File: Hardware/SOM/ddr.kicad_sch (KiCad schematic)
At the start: 25 parts, among them U2 AS4C256M16D3

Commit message: DDR Banks Vref
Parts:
- added C57: 1uF, Capacitor_SMD:C_0402_1005Metric, symbol RA8M1:885012205092
- added C58: 100nF, Capacitor_SMD:C_0402_1005Metric, symbol RA8M1:885012205092
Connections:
- net DDR_VREF: now also C57.2, C58.2
- net GND: now also C57.1, C58.1
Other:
- moved on the sheet: R11, R12, R13, R4, R5

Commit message: SOM: power supplies
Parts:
- removed L1, L2: 600R, Inductor_SMD:L_0402_1005Metric, symbol Device:L
- added FB2, FB3: FerriteBead, Inductor_SMD:L_0402_1005Metric, symbol Device:FerriteBead
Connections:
- net 1.5V: now also FB2.1, FB3.1
- net DDR_VDDQ_1.5V: now also FB2.2
- net DDR_VDD_1.5V: now also FB3.2

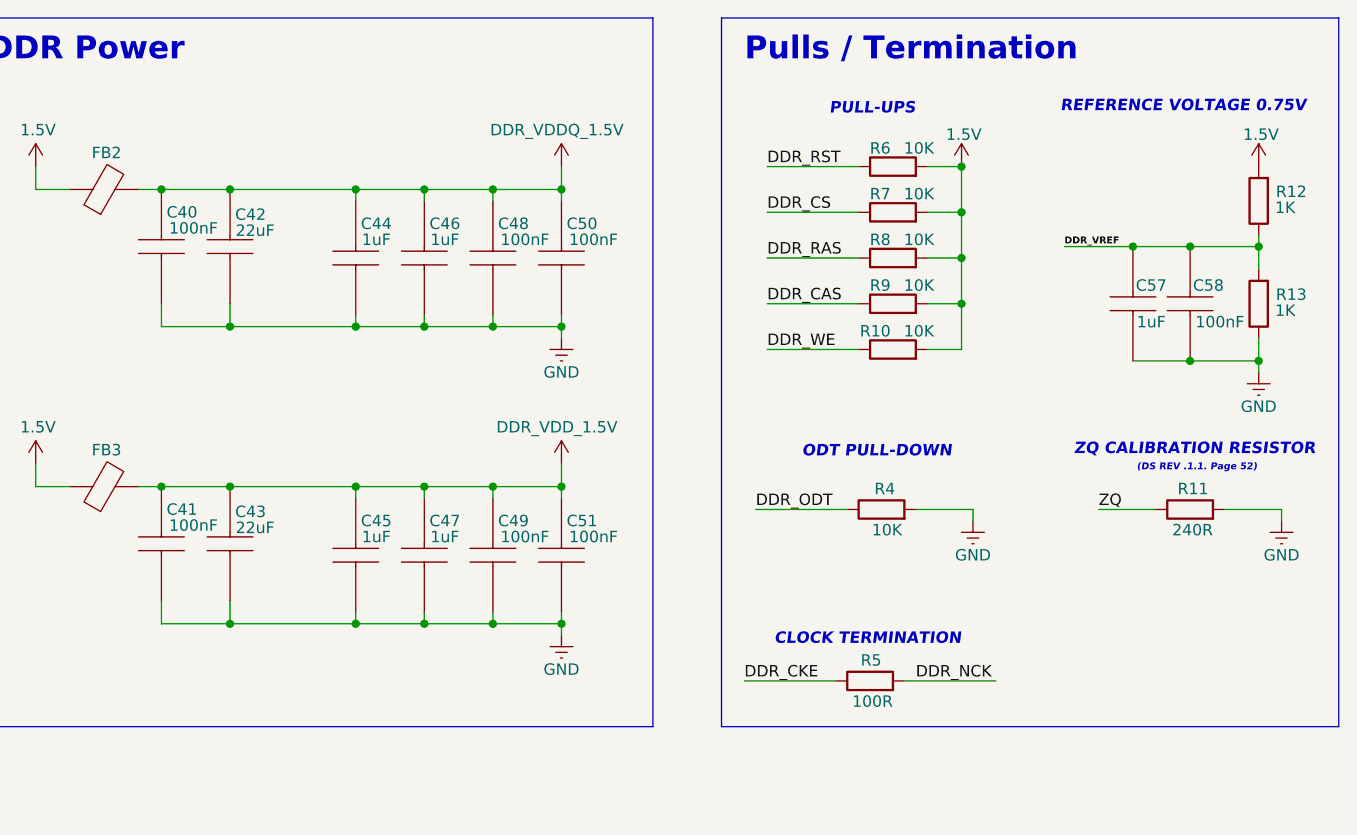
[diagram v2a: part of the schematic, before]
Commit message: SOM: power supply update
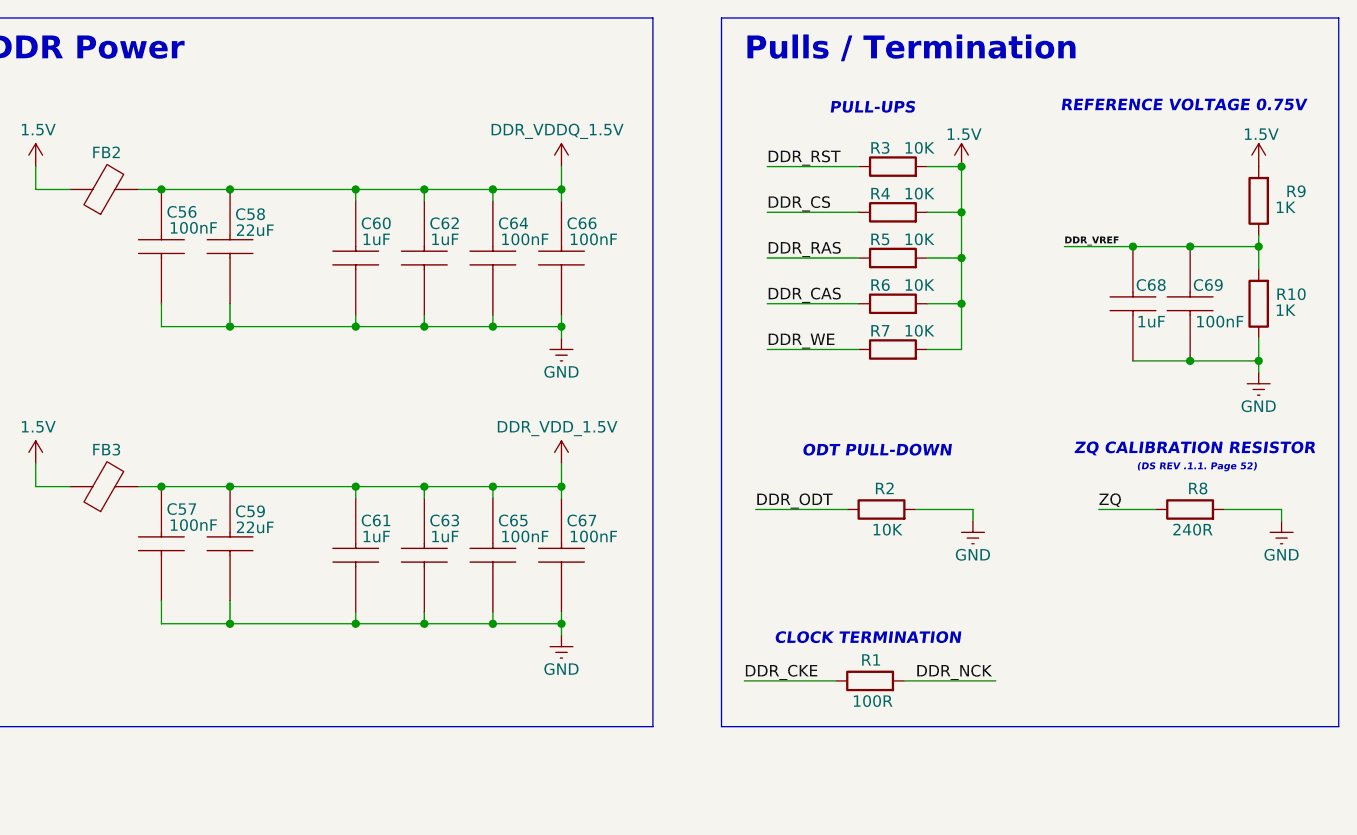
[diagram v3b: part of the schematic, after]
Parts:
- renumbered C40 to C56, C41 to C57, C42 to C58, C43 to C59, C44 to C60, C45 to C61, C46 to C62, C47 to C63, C48 to C64, C49 to C65, C50 to C66, C51 to C67, C57 to C68, C58 to C69, R5 to R1, R13 to R10, R4 to R2, R6 to R3, R7 to R4, R8 to R5, R9 to R6, R10 to R7, R11 to R8, R12 to R9

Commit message: SOM: layout update
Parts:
- renumbered C56 to C76, C57 to C77, C58 to C78, C59 to C79, C60 to C80, C61 to C81, C62 to C82, C63 to C83, C64 to C84, C65 to C85, C66 to C86, C67 to C87, C68 to C88, C69 to C89, FB2 to FB8, FB3 to FB9
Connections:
- net DDR_CKE: no longer U2.K9 (CKE)
- net DDR_NCK: no longer U2.K7 (~{CK})
- new net DDR_CK_N: U2.K7 (~{CK})
- new net DDR_CK_P: U2.K9 (CKE)

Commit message: SOM: layout update
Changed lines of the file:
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@@
 		(dnp no)
 		(property "Reference" "R9"
-			(at 272.034 40.894 0)
+			(at 270.764 40.894 0)
 			(effects
 				(font

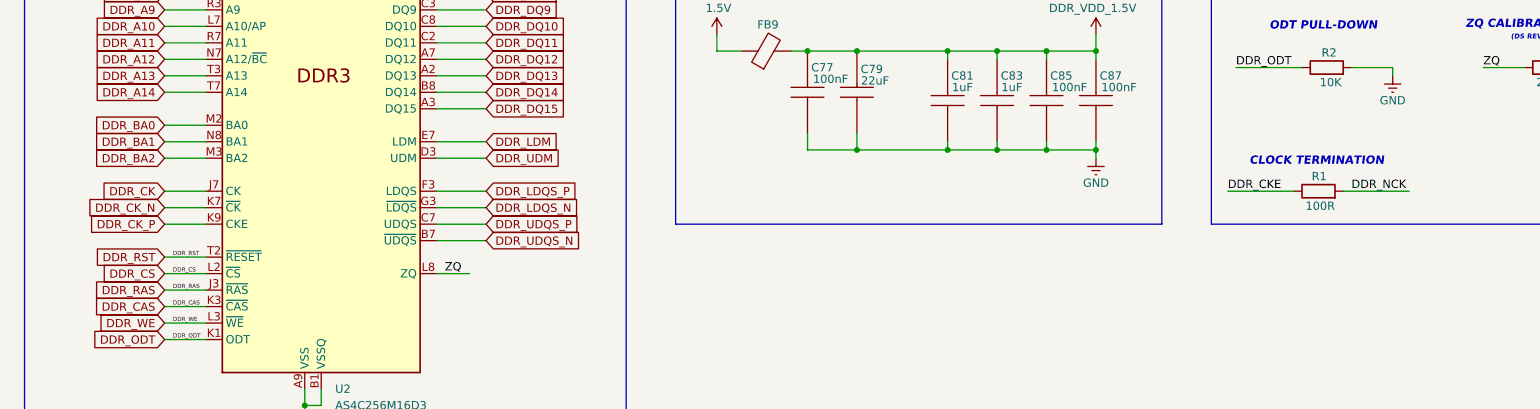
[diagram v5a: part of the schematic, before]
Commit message: DDR clock schematics fixed
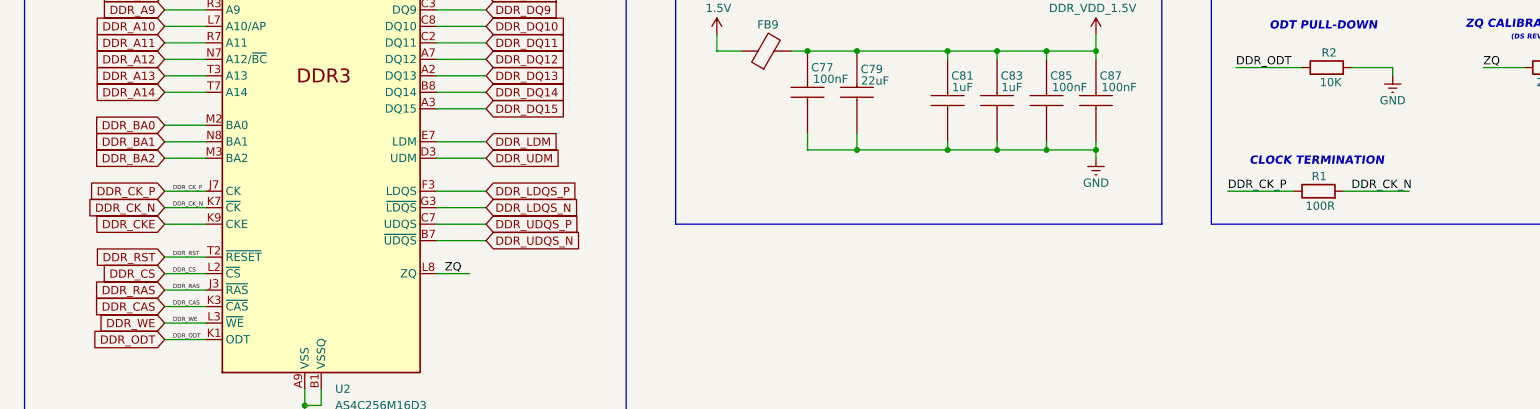
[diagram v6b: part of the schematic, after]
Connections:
- net DDR_CK is gone; now on net DDR_CK_P: U2.J7 (CK)
- net DDR_NCK is gone; now on net DDR_CK_N: R1.2
- net DDR_CKE: now also U2.K9 (CKE); no longer R1.1
- net DDR_CK_P: now also R1.1; no longer U2.K9 (CKE)
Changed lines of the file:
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@@
+		)
+	)
+	(label "DDR_CK_P"
+		(at 46.99 95.25 0)
+		(effects
+			(font
+				(size 0.635 0.635)
+			)
+			(justify left bottom)
 		)
 	)
@@
 		)
 	)
-	(label "DDR_NCK"
+	(label "DDR_CK_N"
+		(at 46.99 97.79 0)
+		(effects
+			(font
+				(size 0.635 0.635)
+			)
+			(justify left bottom)
+		)
+	)
+	(label "DDR_CK_N"
 		(at 228.6 95.25 0)
 		(effects
@@
 		)
 	)
-	(label "DDR_CKE"
+	(label "DDR_CK_P"
 		(at 209.55 95.25 0)
 		(effects
@@
 		)
 	)
+	(global_label "DDR_CKE"
+		(shape input)
+		(at 45.72 100.33 180)
+		(fields_autoplaced yes)
+		(effects
+			(font
+				(size 1.27 1.27)
+			)
+			(justify right)
+		)
+		(property "Intersheetrefs" "${INTERSHEET_REFS}"
+			(at 34.2682 100.33 0)
+			(effects
+				(font
+					(size 1.27 1.27)
+				)
+				(justify right)
+				(hide yes)
+			)
+		)
+	)
+	(global_label "DDR_DQ9"
+		(shape input)
+		(at 95.25 67.31 0)
+		(fields_autoplaced yes)
+		(effects
+			(font
+				(size 1.27 1.27)
+			)
+			(justify left)
+		)
+		(property "Intersheetrefs" "${INTERSHEET_REFS}"
+			(at 106.8228 67.31 0)
+			(effects
+				(font
+					(size 1.27 1.27)
+				)
+				(justify left)
+				(hide yes)
+			)
+		)
+	)
+	(global_label "DDR_DQ13"
+		(shape input)
+		(at 95.25 77.47 0)
+		(fields_autoplaced yes)
+		(effects
+			(font
+				(size 1.27 1.27)
+			)
+			(justify left)
+		)
+		(property "Intersheetrefs" "${INTERSHEET_REFS}"
+			(at 108.0323 77.47 0)
+			(effects
+				(font
+					(size 1.27 1.27)
+				)
+				(justify left)
+				(hide yes)
+			)
+		)
+	)
 	(global_label "DDR_CK_P"
 		(shape input)
-		(at 45.72 100.33 180)
-		(fields_autoplaced yes)
-		(effects
-			(font
-				(size 1.27 1.27)
-			)
-			(justify right)
-		)
-		(property "Intersheetrefs" "${INTERSHEET_REFS}"
-			(at 33.1796 100.33 0)
-			(effects
-				(font
-					(size 1.27 1.27)
-				)
-				(justify right)
-				(hide yes)
-			)
-		)
-	)
-	(global_label "DDR_DQ9"
-		(shape input)
-		(at 95.25 67.31 0)
-		(fields_autoplaced yes)
-		(effects
-			(font
-				(size 1.27 1.27)
-			)
-			(justify left)
-		)
-		(property "Intersheetrefs" "${INTERSHEET_REFS}"
-			(at 106.8228 67.31 0)
-			(effects
-				(font
-					(size 1.27 1.27)
-				)
-				(justify left)
-				(hide yes)
-			)
-		)
-	)
-	(global_label "DDR_DQ13"
-		(shape input)
-		(at 95.25 77.47 0)
-		(fields_autoplaced yes)
-		(effects
-			(font
-				(size 1.27 1.27)
-			)
-			(justify left)
-		)
-		(property "Intersheetrefs" "${INTERSHEET_REFS}"
-			(at 108.0323 77.47 0)
-			(effects
-				(font
-					(size 1.27 1.27)
-				)
-				(justify left)
-				(hide yes)
-			)
-		)
-	)
-	(global_label "DDR_CK"
-		(shape input)
 		(at 45.72 95.25 180)
 		(fields_autoplaced yes)
@@
 		)
 		(property "Intersheetrefs" "${INTERSHEET_REFS}"
-			(at 35.4172 95.25 0)
-			(effects
-				(font
+			(at 33.1796 95.25 0)
+			(effects
+				(font

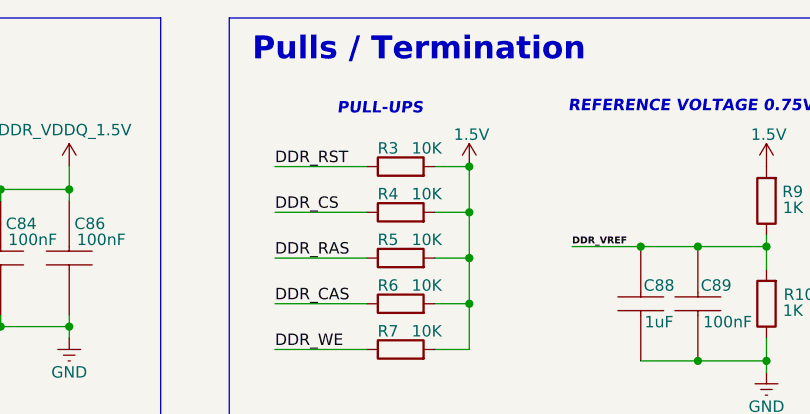
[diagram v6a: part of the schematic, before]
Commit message: SOM: DDR PWR UPD
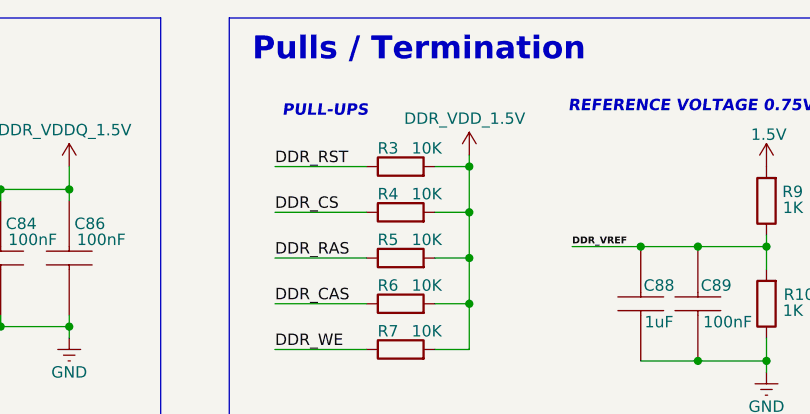
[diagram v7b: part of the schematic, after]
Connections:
- net 1.5V: no longer R3.2, R4.2, R5.2, R6.2, R7.2
- net DDR_VDD_1.5V: now also R3.2, R4.2, R5.2, R6.2, R7.2
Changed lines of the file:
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@@
 	(text "PULL-UPS"
 		(exclude_from_sim no)
-		(at 223.774 31.75 0)
+		(at 217.678 32.004 0)
 		(effects
 			(font
@@
 	)
 	(junction
+		(at 233.68 38.1)
+		(diameter 0)
+		(color 0 0 0 0)
+	)
+	(junction
 		(at 189.23 55.88)
 		(diameter 0)
@@
 	)
 	(junction
-		(at 233.68 38.1)
-		(diameter 0)
-		(color 0 0 0 0)
-	)
-	(junction
 		(at 74.93 35.56)
 		(diameter 0)
@@
 	(wire
 		(pts
+			(xy 233.68 36.83) (xy 233.68 38.1)
+		)
+		(stroke
+			(width 0)
+			(type default)
+		)
+	)
+	(wire
+		(pts
 			(xy 45.72 62.23) (xy 52.07 62.23)
 		)
@@
 	)
 	(symbol
-		(lib_id "power:+1V5")
-		(at 233.68 38.1 0)
-		(unit 1)
-		(exclude_from_sim no)
-		(in_bom yes)
-		(on_board yes)
-		(dnp no)
-		(property "Reference" "#PWR062"
-			(at 233.68 41.91 0)
-			(effects
-				(font
-					(size 1.27 1.27)
-				)
-				(hide yes)
-			)
-		)
-		(property "Value" "1.5V"
-			(at 233.934 34.544 0)
-			(effects
-				(font
-					(size 1.27 1.27)
-				)
-			)
-		)
-		(property "Footprint" ""
-			(at 233.68 38.1 0)
-			(effects
-				(font
-					(size 1.27 1.27)
-				)
-				(hide yes)
-			)
-		)
-		(property "Datasheet" ""
-			(at 233.68 38.1 0)
-			(effects
-				(font
-					(size 1.27 1.27)
-				)
-				(hide yes)
-			)
-		)
-		(property "Description" "Power symbol creates a global label with name \"+1V5\""
-			(at 233.68 38.1 0)
-			(effects
-				(font
-					(size 1.27 1.27)
-				)
-				(hide yes)
-			)
-		)
-		(pin "1"
-		)
-		(instances
-			(project "LFE5UM5G-85F_SOM"
-				(path "/de32abb0-ff3b-4c67-a91a-eed08140b1b2/70285655-daa5-4a1b-b29b-80c93a345d65"
-					(reference "#PWR062")
-					(unit 1)
-				)
-			)
-		)
-	)
-	(symbol
 		(lib_id "Memory_RAM:AS4C256M16D3")
 		(at 69.85 82.55 0)
@@
 					(unit 1)
 				)
+			)
+		)
+	)
+	(symbol
+		(lib_id "power:+1V5")
+		(at 233.68 36.83 0)
+		(unit 1)
+		(exclude_from_sim no)
+		(in_bom yes)
+		(on_board yes)
+		(dnp no)
+		(property "Reference" "#PWR010"
+			(at 233.68 40.64 0)
+			(effects
+				(font
+					(size 1.27 1.27)
+				)
+				(hide yes)
+			)
+		)
+		(property "Value" "DDR_VDD_1.5V"
+			(at 233.172 32.766 0)
+			(effects
+				(font
+					(size 1.27 1.27)
+				)
+			)
+		)
+		(property "Footprint" ""
+			(at 233.68 36.83 0)
+			(effects
+				(font
+					(size 1.27 1.27)
+				)
+				(hide yes)
+			)
+		)
+		(property "Datasheet" ""
+			(at 233.68 36.83 0)
+			(effects
+				(font
+					(size 1.27 1.27)
+				)
+				(hide yes)
+			)
+		)
+		(property "Description" "Power symbol creates a global label with name \"+1V5\""
+			(at 233.68 36.83 0)
+			(effects
+				(font
+					(size 1.27 1.27)
+				)
+				(hide yes)
+			)
+		)
+		(pin "1"
+		)
+		(instances
+			(project "LFE5UM5G-85F_SOM"
+				(path "/de32abb0-ff3b-4c67-a91a-eed08140b1b2/70285655-daa5-4a1b-b29b-80c93a345d65"
+					(reference "#PWR010")
+					(unit 1)
+				)
